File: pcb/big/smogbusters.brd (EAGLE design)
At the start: 68.6 x 65.7 mm, 22 parts, among them Q1 IRLZ44N

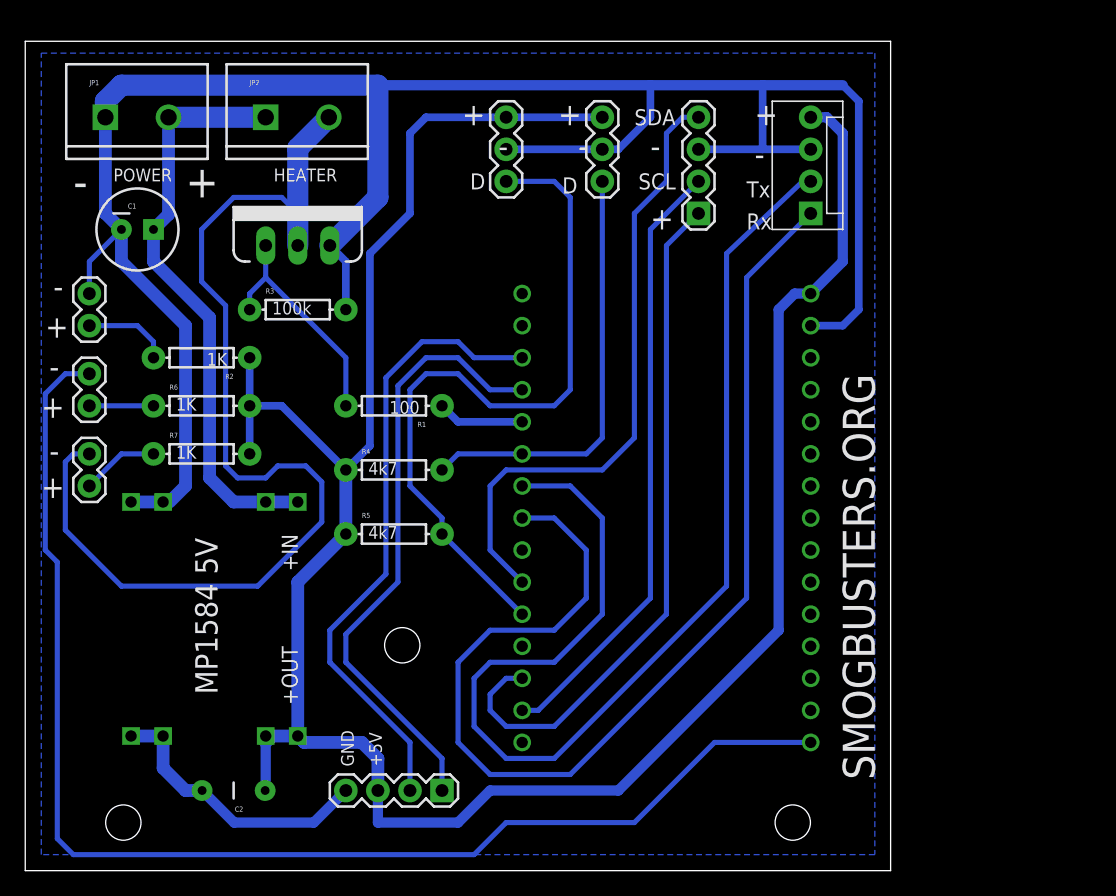
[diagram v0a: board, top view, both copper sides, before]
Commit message: PCB fixes acc. to ticket #1
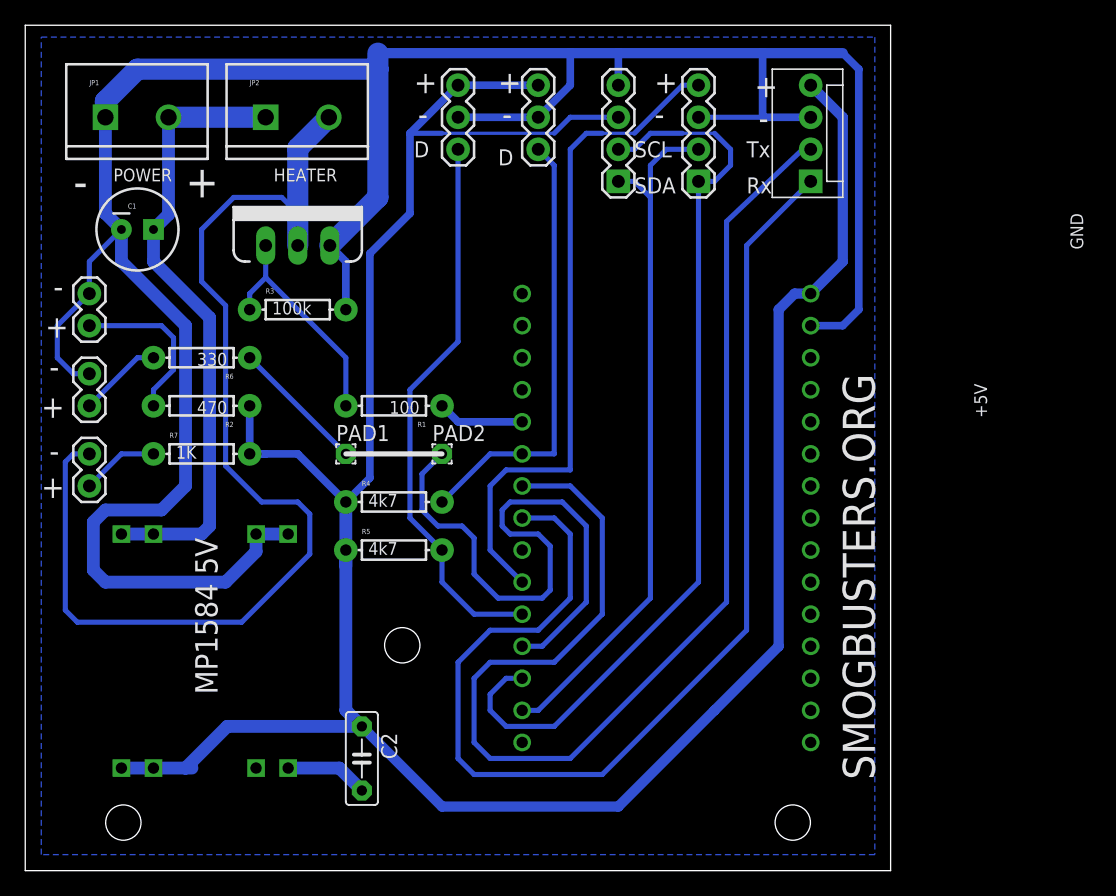
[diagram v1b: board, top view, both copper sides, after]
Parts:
- added PAD1, PAD2: (no value), wirepad:1,6/0,8
- C2: value 100nF -> 100n; device SparkFun-Capacitors:CAP-PTH-5MM -> capacitor-wima:C5B2.5
- R2: value 1K -> 470
- R6: value 1K -> 330
- moved JP10 50.2 mm to (47.0, 53.3), turned to 90 degrees
- moved U$2 14.2 mm to (7.62, 25.4), flipped to the bottom
- moved C2 10.5 mm to (26.7, 7.62), turned to 270 degrees
- moved JP6 5.68 mm to (40.6, 55.9)
- moved JP7 4.58 mm to (34.3, 55.9)
- moved R2 3.81 mm to (14.0, 35.6)
- moved R6 3.81 mm to (14.0, 39.4), turned to 180 degrees
- moved JP3 2.54 mm to (53.3, 53.3)
- moved JP8 2.54 mm to (62.2, 53.3)
- moved R4 2.54 mm to (29.2, 27.9)
- moved R5 1.27 mm to (29.2, 24.1)
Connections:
- removed net N$10: JP3.1, U$1.P$28
- removed net N$11: JP3.2, U$1.P$29
- new net N$4: JP5.1, R6.P$2
- net +5V: no longer R6.P$2
- net GND: now also JP5.2
- net N$12: now also PAD1.1; no longer JP5.1
- net N$14: now also PAD2.1, U$1.P$27; no longer JP5.2, U$1.P$1
- net N$16: now also JP10.2, JP3.1, U$1.P$28; no longer JP10.1, U$1.P$19
- net N$17: now also JP10.1, JP3.2, U$1.P$29; no longer JP10.2, U$1.P$18
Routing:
- net N$10: track 55.3 -> 0.00 mm
- net N$14: track 103.7 -> 49.6 mm
- net N$11: track 48.4 -> 0.00 mm
- net GND: track 197.0 -> 221.6 mm
- net N$16: track 48.7 -> 72.1 mm
- net +5V: track 187.1 -> 204.1 mm
- net N$9: track 57.1 -> 44.3 mm
- net N$4: track 0.00 -> 6.66 mm
- net N$15: track 6.88 -> 13.1 mm
- net N$17: track 49.7 -> 55.5 mm
- net N$12: track 5.08 -> 10.8 mm
- net N$7: track 93.1 -> 97.4 mm
- net N$1: track 83.8 -> 87.2 mm
- net N$5: track 49.9 -> 53.2 mm
- net +12V: track 46.4 -> 49.7 mm
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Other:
- board size 68.6 x 65.7 mm -> 68.6 x 67 mm
